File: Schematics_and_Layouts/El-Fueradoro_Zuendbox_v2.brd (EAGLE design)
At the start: 157.5 x 97.5 mm, 139 parts, among them IC1 MAX202, IC2 MEGA168P/328P, IC6 74HC595N, IC7 74HC595N, IC8 LM1086IT-3.3, Q1 9.8304, Q10 IRF3708, Q11 IRF3708, Q12 IRF3708, Q13 IRF3708, Q14 IRF3708, Q15 IRF3708, Q16 IRF3708, Q17 IRF3708, Q18 BC337, Q19 IRF4905, Q2 IRF3708, Q3 IRF3708, Q4 IRF3708, Q5 IRF3708, Q6 IRF3708, Q7 IRF3708, Q8 IRF3708, Q9 IRF3708, T1 BC337, T2 BC 327

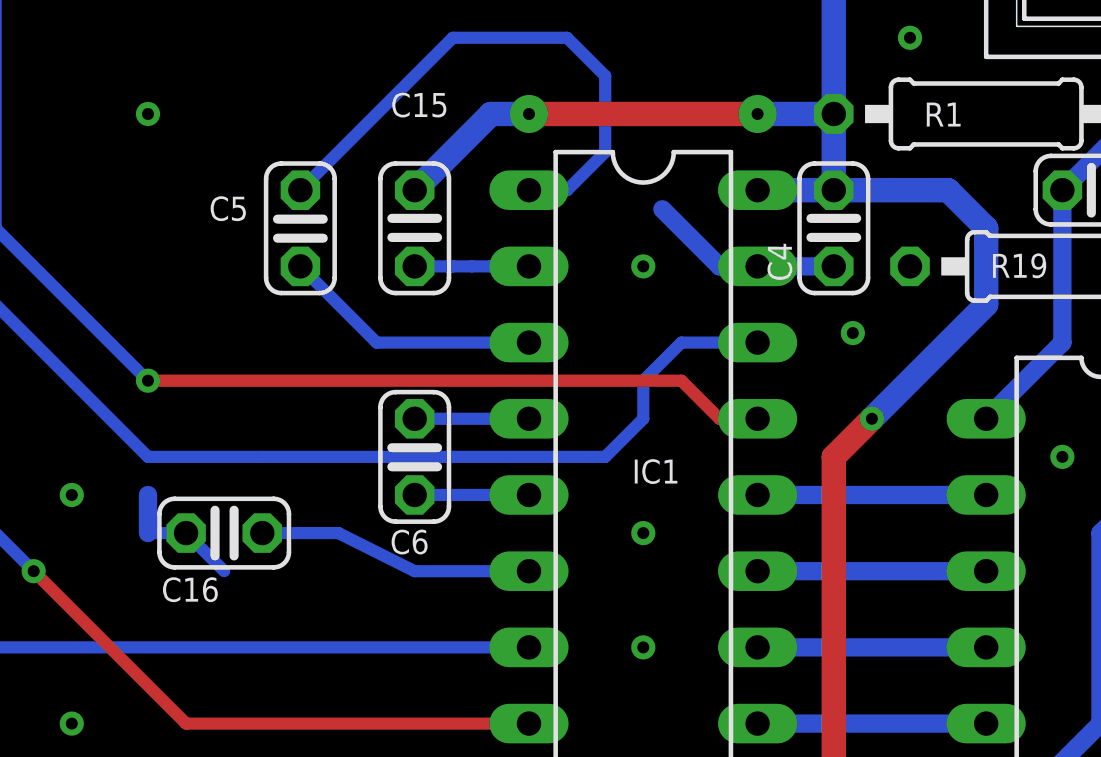
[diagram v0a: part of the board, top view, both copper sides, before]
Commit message: Bugfix in Zündbox_v2-Gerber-Files Kompiliert mit AVR-GCC 8
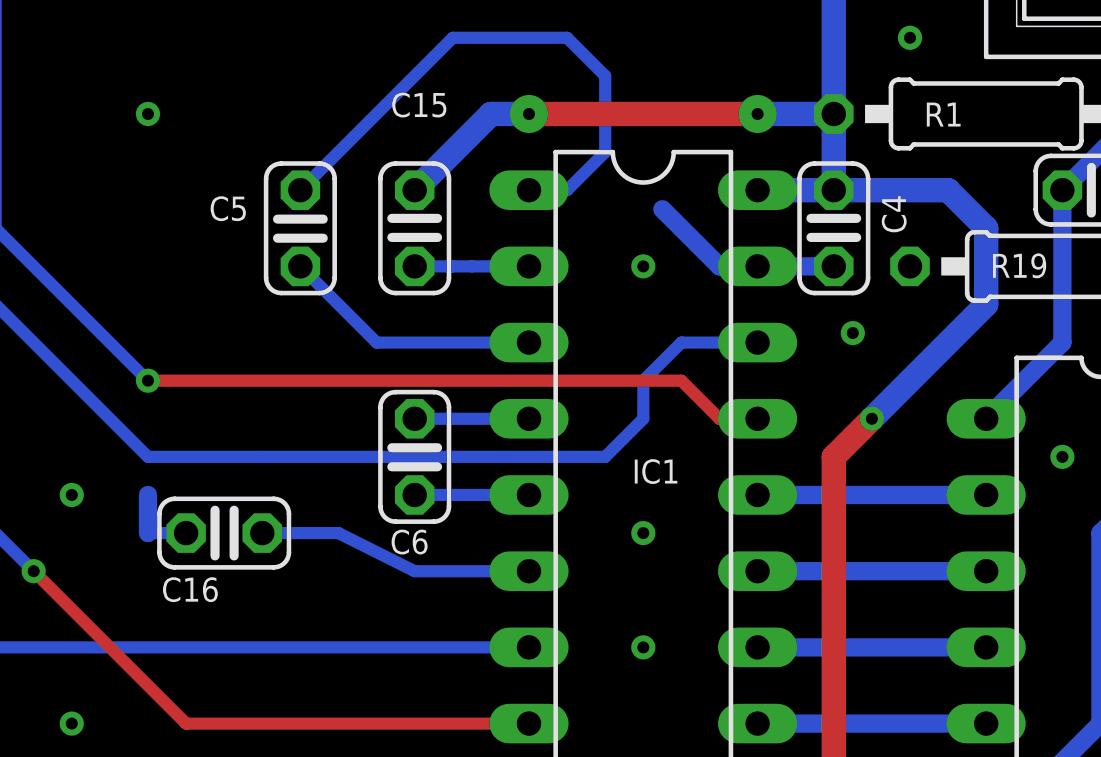
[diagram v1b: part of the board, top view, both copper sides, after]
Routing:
- net GND: track 21.0 -> 19.2 mm
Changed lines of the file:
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@@
 </element>
 <element name="C4" library="rcl" package="C025-024X044" value="100n" x="38.1" y="52.07" smashed="yes" rot="R90">
-<attribute name="NAME" x="36.703" y="50.292" size="0.8" layer="25" font="vector" ratio="20" rot="R90"/>
-<attribute name="VALUE" x="40.767" y="50.292" size="0.8" layer="27" font="vector" ratio="20" rot="R90"/>
+<attribute name="NAME" x="40.513" y="51.8795" size="0.8" layer="25" font="vector" ratio="20" rot="R90"/>
+<attribute name="VALUE" x="41.402" y="51.8795" size="0.8" layer="27" font="vector" ratio="20" rot="R90"/>
 </element>
 <element name="C5" library="rcl" package="C025-024X044" value="100n" x="20.32" y="52.07" smashed="yes" rot="R270">
@@
 </element>
 <element name="C8" library="rcl" package="C025-024X044" value="15p" x="29.21" y="25.4" smashed="yes">
-<attribute name="NAME" x="24.892" y="25.8445" size="0.8" layer="25" ratio="20"/>
-<attribute name="VALUE" x="24.5745" y="24.9555" size="0.8" layer="27" ratio="20"/>
+<attribute name="NAME" x="24.892" y="25.8445" size="0.8" layer="25" font="vector" ratio="20"/>
+<attribute name="VALUE" x="24.5745" y="24.9555" size="0.8" layer="27" font="vector" ratio="20"/>
 </element>
 <element name="C9" library="rcl" package="C025-024X044" value="15p" x="29.21" y="22.86" smashed="yes">
-<attribute name="NAME" x="24.892" y="22.987" size="0.8" layer="25" ratio="20"/>
-<attribute name="VALUE" x="24.5745" y="22.098" size="0.8" layer="27" ratio="20"/>
+<attribute name="NAME" x="24.892" y="22.987" size="0.8" layer="25" font="vector" ratio="20"/>
+<attribute name="VALUE" x="24.5745" y="22.098" size="0.8" layer="27" font="vector" ratio="20"/>
 </element>
 <element name="R8" library="rcl" package="0207/10" value="1k" x="33.02" y="10.16" smashed="yes">
-<attribute name="NAME" x="30.607" y="9.779" size="0.8" layer="25" ratio="20"/>
-<attribute name="VALUE" x="34.2519" y="9.8425" size="0.8" layer="27" ratio="20"/>
+<attribute name="NAME" x="30.607" y="9.779" size="0.8" layer="25" font="vector" ratio="20"/>
+<attribute name="VALUE" x="34.2519" y="9.8425" size="0.8" layer="27" font="vector" ratio="20"/>
 </element>
 <element name="R9" library="rcl" package="0207/10" value="1k" x="33.02" y="12.7" smashed="yes">
-<attribute name="NAME" x="30.607" y="12.319" size="0.8" layer="25" ratio="20"/>
-<attribute name="VALUE" x="34.2519" y="12.3825" size="0.8" layer="27" ratio="20"/>
+<attribute name="NAME" x="30.607" y="12.319" size="0.8" layer="25" font="vector" ratio="20"/>
+<attribute name="VALUE" x="34.2519" y="12.3825" size="0.8" layer="27" font="vector" ratio="20"/>
 </element>
 <element name="R10" library="rcl" package="0207/10" value="1k" x="33.02" y="15.24" smashed="yes">
-<attribute name="NAME" x="30.607" y="14.859" size="0.8" layer="25" ratio="20"/>
-<attribute name="VALUE" x="34.2519" y="14.9225" size="0.8" layer="27" ratio="20"/>
+<attribute name="NAME" x="30.607" y="14.859" size="0.8" layer="25" font="vector" ratio="20"/>
+<attribute name="VALUE" x="34.2519" y="14.9225" size="0.8" layer="27" font="vector" ratio="20"/>
 </element>
 <element name="R11" library="rcl" package="0207/10" value="1k" x="33.02" y="17.78" smashed="yes">
-<attribute name="NAME" x="30.607" y="17.399" size="0.8" layer="25" ratio="20"/>
-<attribute name="VALUE" x="34.2519" y="17.4625" size="0.8" layer="27" ratio="20"/>
+<attribute name="NAME" x="30.607" y="17.399" size="0.8" layer="25" font="vector" ratio="20"/>
+<attribute name="VALUE" x="34.2519" y="17.4625" size="0.8" layer="27" font="vector" ratio="20"/>
 </element>
 <element name="LED_O" library="led" package="LED5MM" value="" x="20.32" y="17.78" smashed="yes" rot="R180">
@@
 <element name="U$4" library="fp" package="RFM69CW" value="RFM69CW" x="78.74" y="40.64" smashed="yes" rot="R270"/>
 <element name="R13" library="rcl" package="0207/10" value="270R" x="60.96" y="81.28" smashed="yes" rot="R90">
-<attribute name="NAME" x="61.341" y="78.5495" size="0.8" layer="25" ratio="20" rot="R90"/>
-<attribute name="VALUE" x="61.2775" y="81.5594" size="0.8" layer="27" ratio="20" rot="R90"/>
+<attribute name="NAME" x="61.341" y="78.5495" size="0.8" layer="25" font="vector" ratio="20" rot="R90"/>
+<attribute name="VALUE" x="61.2775" y="81.5594" size="0.8" layer="27" font="vector" ratio="20" rot="R90"/>
 </element>
 <element name="Q18" library="transistor-npn" package="TO92" value="BC337" x="66.04" y="76.2" smashed="yes" rot="R180">
-<attribute name="NAME" x="68.58" y="73.9775" size="0.8" layer="25" ratio="20"/>
-<attribute name="VALUE" x="67.6275" y="73.025" size="0.8" layer="27" ratio="20"/>
+<attribute name="NAME" x="68.58" y="73.9775" size="0.8" layer="25" font="vector" ratio="20"/>
+<attribute name="VALUE" x="67.6275" y="73.025" size="0.8" layer="27" font="vector" ratio="20"/>
 </element>
 <element name="R14" library="rcl" package="0207/10" value="1k5" x="73.66" y="81.28" smashed="yes" rot="R270">
-<attribute name="NAME" x="73.279" y="81.153" size="0.8" layer="25" ratio="20" rot="R270"/>
-<attribute name="VALUE" x="73.3425" y="84.1756" size="0.8" layer="27" ratio="20" rot="R270"/>
+<attribute name="NAME" x="73.279" y="81.153" size="0.8" layer="25" font="vector" ratio="20" rot="R270"/>
+<attribute name="VALUE" x="73.3425" y="84.1756" size="0.8" layer="27" font="vector" ratio="20" rot="R270"/>
 </element>
 <element name="R16" library="rcl" package="0207/10" value="10k" x="35.56" y="33.02" smashed="yes">
-<attribute name="NAME" x="28.3845" y="30.734" size="0.8" layer="25" ratio="20"/>
-<attribute name="VALUE" x="28.2194" y="29.845" size="0.8" layer="27" ratio="20"/>
+<attribute name="NAME" x="28.3845" y="30.734" size="0.8" layer="25" font="vector" ratio="20"/>
+<attribute name="VALUE" x="28.2194" y="29.845" size="0.8" layer="27" font="vector" ratio="20"/>
 </element>
 <element name="Q19" library="transistor-power" package="TO220BV" value="IRF4905" x="114.3" y="76.2" smashed="yes">
-<attribute name="NAME" x="106.68" y="73.6473" size="0.8" layer="25" ratio="20"/>
-<attribute name="VALUE" x="104.14" y="72.39" size="0.8" layer="27" ratio="20"/>
+<attribute name="NAME" x="106.68" y="73.6473" size="0.8" layer="25" font="vector" ratio="20"/>
+<attribute name="VALUE" x="104.14" y="72.39" size="0.8" layer="27" font="vector" ratio="20"/>
 </element>
 <element name="R_Z1" library="resistor-power" package="KH214R-8" value="150R" x="116.5225" y="84.1375" smashed="yes" rot="R90">
@@
 <attribute name="MF" value="" x="116.5225" y="84.1375" size="1.778" layer="27" rot="R90" display="off"/>
 <attribute name="OC_FARNELL" value="unknown" x="116.5225" y="84.1375" size="1.778" layer="27" rot="R90" display="off"/>
-<attribute name="NAME" x="113.284" y="77.7875" size="0.8" layer="25" ratio="20" rot="R90"/>
-<attribute name="VALUE" x="114.4905" y="77.7875" size="0.8" layer="27" ratio="20" rot="R90"/>
+<attribute name="NAME" x="113.284" y="77.7875" size="0.8" layer="25" font="vector" ratio="20" rot="R90"/>
+<attribute name="VALUE" x="114.4905" y="77.7875" size="0.8" layer="27" font="vector" ratio="20" rot="R90"/>
 </element>
 <element name="R17" library="rcl" package="0207/10" value="dnp" x="81.28" y="50.8" smashed="yes">
-<attribute name="NAME" x="78.5495" y="50.419" size="0.8" layer="25" ratio="20"/>
-<attribute name="VALUE" x="82.1944" y="50.4825" size="0.8" layer="27" ratio="20"/>
+<attribute name="NAME" x="78.5495" y="50.419" size="0.8" layer="25" font="vector" ratio="20"/>
+<attribute name="VALUE" x="82.1944" y="50.4825" size="0.8" layer="27" font="vector" ratio="20"/>
 </element>
 <element name="T1" library="transistor" package="TO92" value="BC337" x="83.82" y="81.28" smashed="yes" rot="R270">
@@
 <contactref element="R19" pad="1"/>
 <wire x1="15.24" y1="41.91" x2="16.51" y2="41.91" width="0.4064" layer="16"/>
-<wire x1="16.51" y1="41.91" x2="17.78" y2="40.64" width="0.4064" layer="16"/>
 <contactref element="R20" pad="2"/>
 <contactref element="R37" pad="1"/>

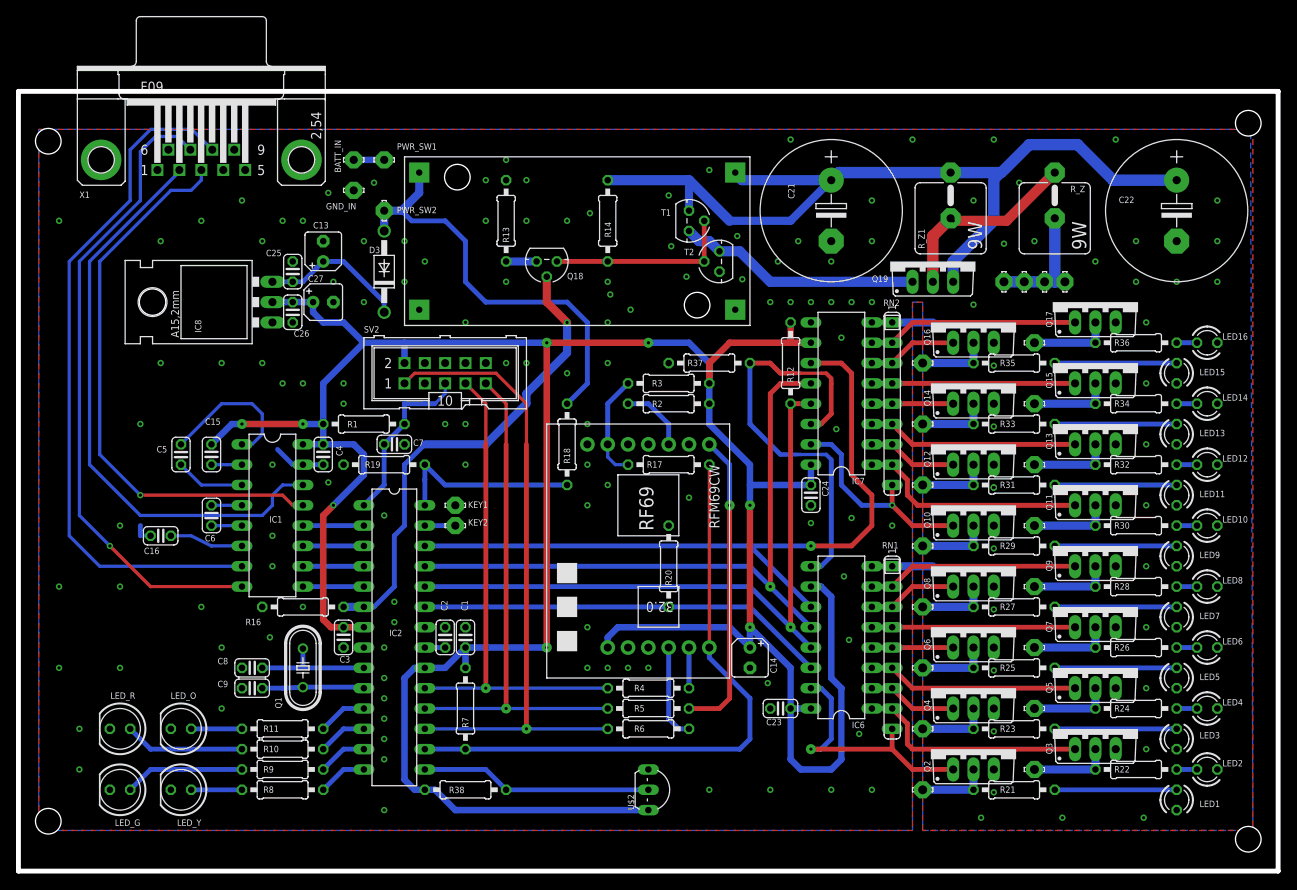
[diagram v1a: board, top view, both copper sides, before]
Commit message: Angleichung von Handbuch und Layouts
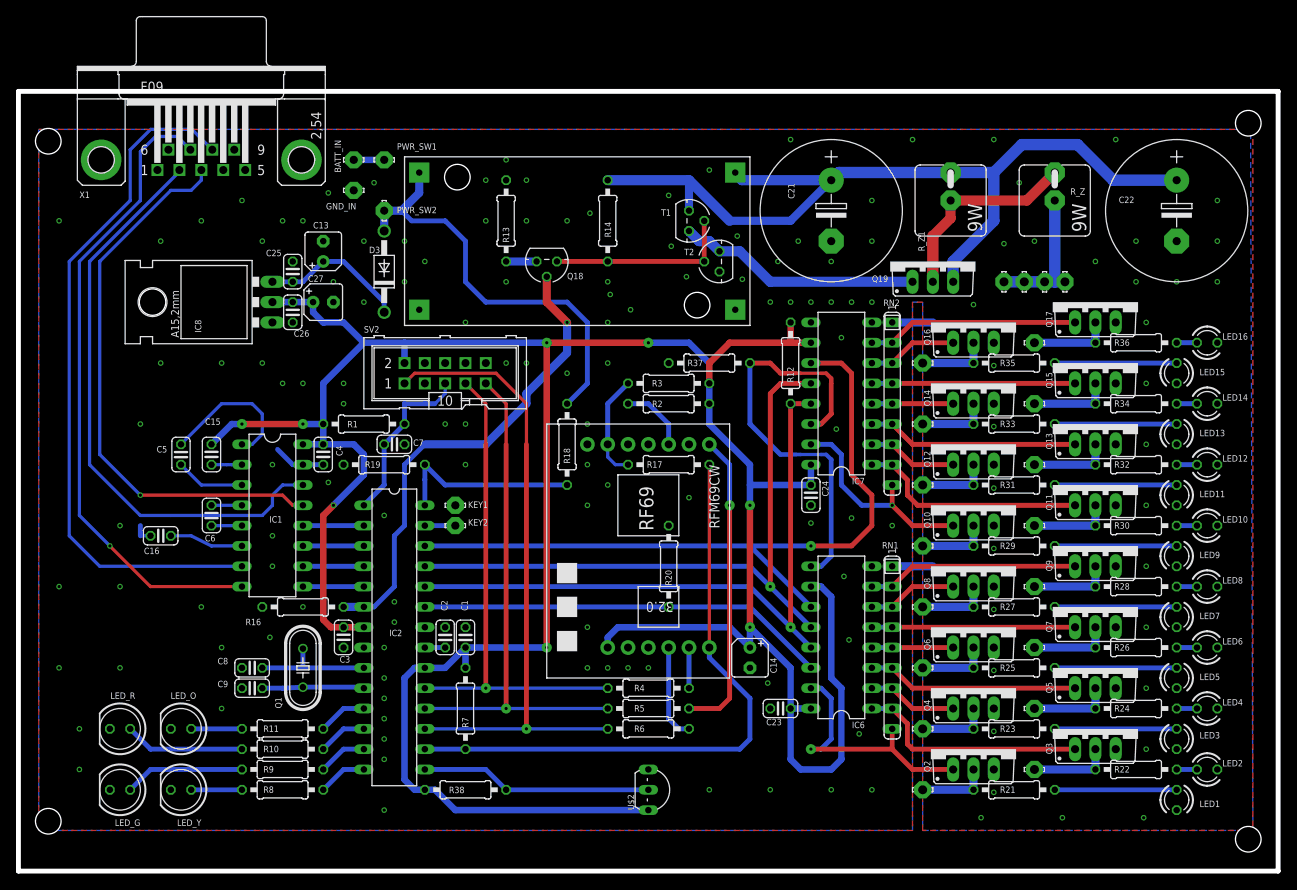
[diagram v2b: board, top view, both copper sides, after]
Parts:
- D3: value 1N4004 -> 1N4002
- R4, R5, R6: value 2k2 -> 1k
- moved R_Z 0.32 mm to (129.5, 83.8)
- moved R_Z1 0.32 mm to (116.5, 83.8)
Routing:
- net N$7: track 15.6 -> 17.8 mm
- net N$8: track 24.5 -> 25.6 mm, vias 1 -> 0
- net GND: vias 145 -> 143
